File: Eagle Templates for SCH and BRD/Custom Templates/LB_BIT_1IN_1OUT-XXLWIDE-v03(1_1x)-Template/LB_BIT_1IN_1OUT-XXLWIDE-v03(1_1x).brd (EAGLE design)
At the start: 44.4 x 51.2 mm, 17 parts, among them U1 LV321SOT23-5, U2 LV321SOT23-5

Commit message: added bitlab logo and made minor changes to board templates. Updated littlebits library.
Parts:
- added U$5: (no value), LITTLEBITS:BITLAB-LOGO
- renumbered FRAME1 to U$3
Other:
- board text added: "iX Name Here"
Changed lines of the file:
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@@
 <layer number="113" name="extra" color="10" fill="1" visible="yes" active="yes"/>
 <layer number="116" name="Patch_BOT" color="9" fill="4" visible="yes" active="yes"/>
+<layer number="118" name="Rect_Pads" color="7" fill="1" visible="no" active="yes"/>
 <layer number="121" name="_tsilk" color="7" fill="1" visible="yes" active="yes"/>
 <layer number="122" name="_bsilk" color="7" fill="1" visible="yes" active="yes"/>
@@
 <wire x1="-17.548" y1="8.165" x2="-17.55" y2="8.165" width="0" layer="20" curve="-0.045837"/>
 <text x="24.5" y="6.1" size="0.8128" layer="16" font="vector" ratio="12" rot="MR90">revX</text>
+<text x="23.6" y="29.7195" size="1.3" layer="21" font="vector" rot="SR270" align="center">iX Name Here</text>
 </plain>
 <attributes>
@@
 </element>
 <element name="U$4" library="ohw-logo" package="OSHW_FILLX150_NOTEXT" value="" x="21.5" y="49.1" rot="MR90"/>
-<element name="FRAME1" library="LITTLEBITS" package="FABDWG01-OHW" value="FRAME-LETTER" x="0" y="0"/>
+<element name="U$5" library="LITTLEBITS" package="BITLAB-LOGO" value="" x="22.3" y="33.1" rot="R270"/>
+<element name="U$3" library="LITTLEBITS" package="FABDWG01-OHW" value="FRAME-LETTER" x="0" y="0"/>
 </elements>
 <signals>

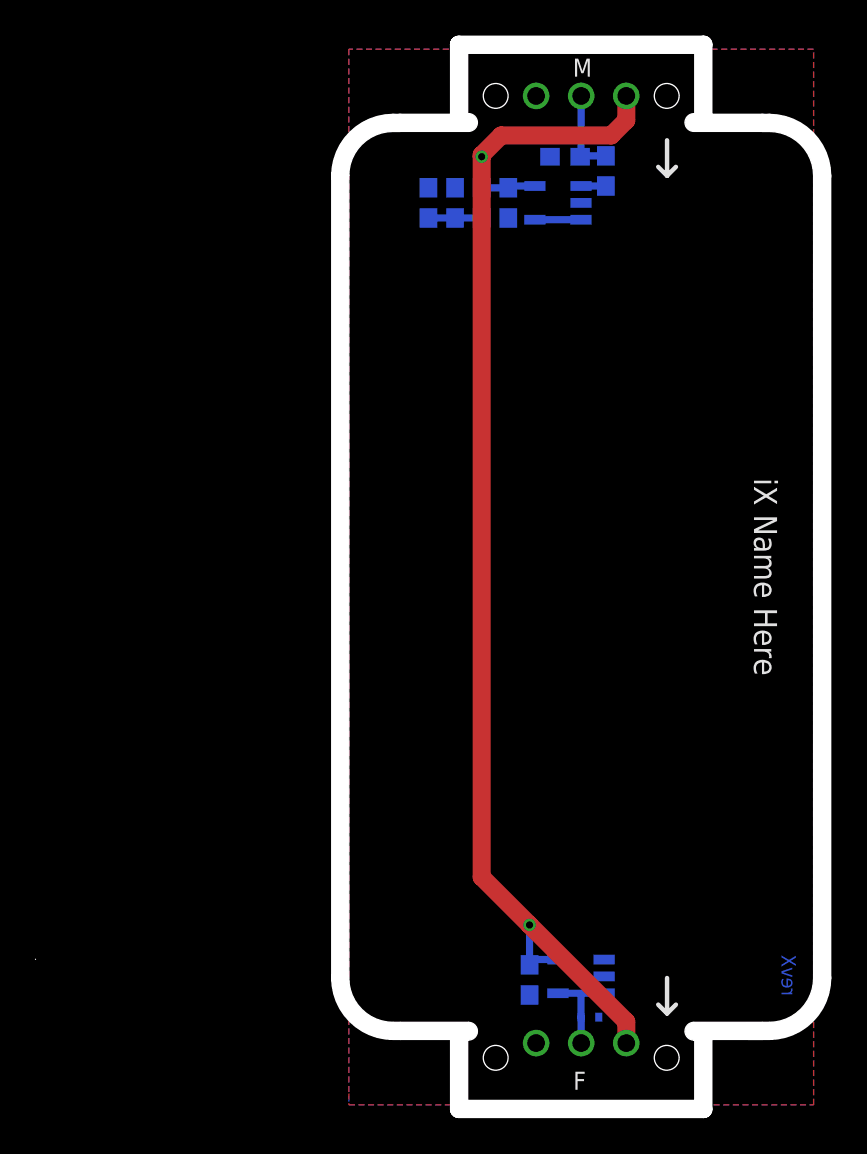
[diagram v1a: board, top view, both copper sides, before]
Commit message: Updated templates
- Added ferrite beads
- Moved text and annotations off of Nets layer
- Minor layout changes
- Removed I/O/W prefix from reference designators
- Removed output stage components from output bits
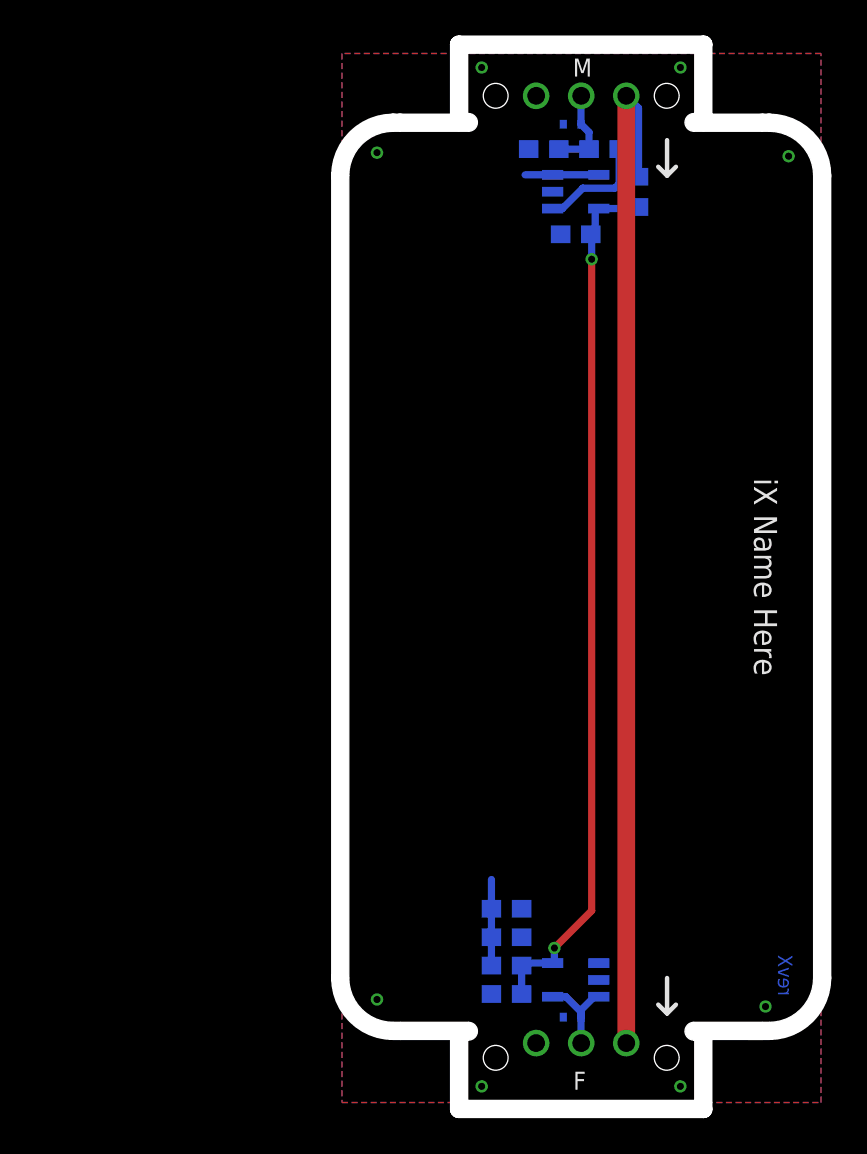
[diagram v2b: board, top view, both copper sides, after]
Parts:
- removed I?BSM: BITSNAP_V03_MALE, bitSnap:BITSNAP_V03_MALE
- removed I?C1: 0.1uF, LITTLEBITS:CAP-0603
- removed I?C2: 10uF, LITTLEBITS:CAP-0603
- removed I?C3: 1.0uF, LITTLEBITS:CAP-0603
- removed I?R1: 1meg, LITTLEBITS:RES-0603
- removed I?R2: 10K, LITTLEBITS:RES-0603
- removed I?R3, I?R4: 3K3, LITTLEBITS:RES-0603
- removed I?TVS1, I?TVS2: ESD9B5.0ST5G, LITTLEBITS:SOD-923
- added BSM1: BITSNAP_V03_MALE, bitSnap:BITSNAP_V03_MALE
- added C1: 0.1uF, LITTLEBITS:CAP-0603
- added C2: 10uF, LITTLEBITS:CAP-0603
- added C3: 1.0uF, LITTLEBITS:CAP-0603
- added FB1: FERRITE-BEAD0603, LITTLEBITS:R0603
- added R1: 1meg, LITTLEBITS:RES-0603
- added R2: 10K, LITTLEBITS:RES-0603
- added R3, R4: 3K3, LITTLEBITS:RES-0603
- added TVS1, TVS2: ESD9B5.0ST5G, LITTLEBITS:SOD-923
- U$1: value OSHWCREDIT -> OSHW-LOGOL; device LITTLEBITS:OSHWCREDIT -> LITTLEBITS131206:OSHW-LOGO-L
- U$2: value OSHW-LOGOL -> OSHWCREDIT; device LITTLEBITS131206:OSHW-LOGO-L -> LITTLEBITS:OSHWCREDIT
- U$3: value FRAME-LETTER -> (none); device LITTLEBITS:FABDWG01-OHW -> LITTLEBITS:BITLAB-LOGO
- U$5: value (none) -> FRAME-LETTER-OHWOHW; device LITTLEBITS:BITLAB-LOGO -> LITTLEBITS:FABDWG01-OHW
- moved U$2 61.9 mm to (-92.2, -64.3)
- moved U$1 50.2 mm to (-37.5, -68.2)
- moved U$3 39.9 mm to (22.3, 33.1), turned to 270 degrees
- moved U$5 39.9 mm to (0.00, 0.00), turned to 0 degrees
- moved U1 1.18 mm to (12.9, 51.4), turned to 90 degrees
- moved U2 0.36 mm to (12.9, 7.00)
- renumbered I?BSF to BSF1
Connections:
- removed net N$9: I?R2.1, U1.1
- new net LB_VCC: BSF1.VCC, BSM1.VCC1, FB1.2
- new net N$4: R2.1, U1.1
- net GND: now also BSM1.GND1, C1.2, C2.2, C3.1, R1.1, R4.1, TVS1.1, TVS2.1; no longer I?BSM.GND1, I?C1.2, I?C2.2, I?C3.1, I?R1.1, I?R4.1, I?TVS1.1, I?TVS2.1
- net SIG_IN: now also BSM1.SIG1, R1.2, R2.2, TVS1.2; no longer I?BSM.SIG1, I?R1.2, I?R2.2, I?TVS1.2
- net SIG_OUT: now also TVS2.2; no longer I?TVS2.2
- net VCC: now also C1.1, C3.2, FB1.1, R3.2; no longer BSF1.VCC, I?BSM.VCC1, I?C1.1, I?C3.2, I?R3.2
- net VREF: now also C2.1, R3.1, R4.2; no longer I?C2.1, I?R3.1, I?R4.2
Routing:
- net LB_VCC: track 0.00 -> 58.2 mm
- net VCC: track 72.5 -> 50.1 mm
- net N$4: track 0.00 -> 6.28 mm
- net VREF: track 3.00 -> 4.85 mm
- net N$2: track 2.60 -> 4.15 mm
- net N$9: track 1.40 -> 0.00 mm
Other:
- board size 44.4 x 51.2 mm -> 27.2 x 51.2 mm
